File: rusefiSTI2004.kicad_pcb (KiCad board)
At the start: 2 copper layers, 138.6 x 113.6 mm, 35 parts, among them J1 1-1376430-0, M1 Module-mega-mcu144-0.7, M13 Module-knock-0.2, M14 Module-power_12and5V-0.3, M2 Module-motor-driver-0.1, M3 Module-wbo-0.5, M4 Module-can-0.1, M5 Module-vr-discrete-0.5, M6 Module-vr-discrete-0.5, M7 Module-knock-0.2, M8 Module-power_12and5V-0.3, M9 Module-motor-driver-0.1, Q1 VND14NV04-E, Q2 VND14NV04-E, Q3 VND14NV04-E, Q4 VND14NV04-E, Q5 VND14NV04-E, Q6 VND14NV04-E, Q7 VND14NV04-E, Q8 VND14NV04-E

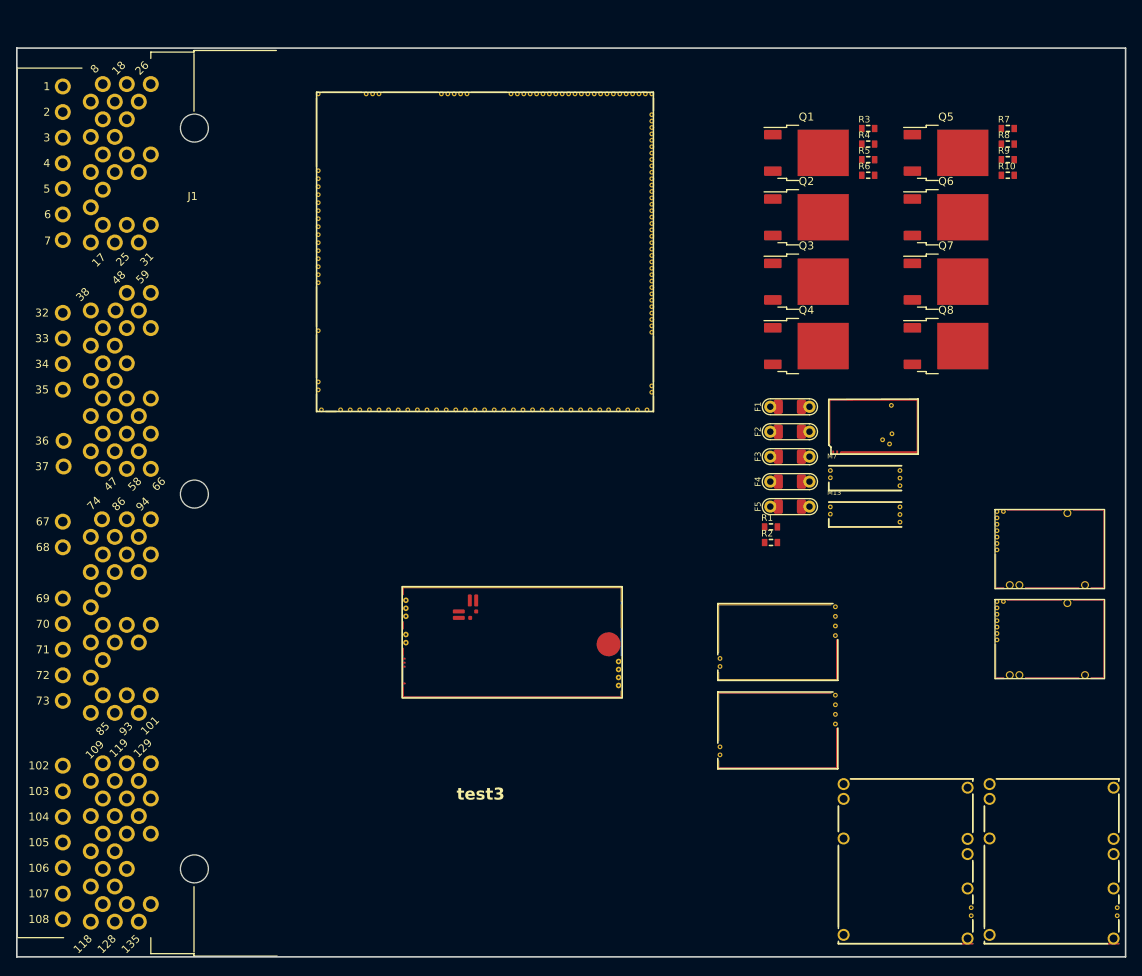
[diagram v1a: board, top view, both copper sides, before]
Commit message: PCB: update from schematic and first placement; H1-H4 M3 mounting holes; drop STI.pretty
- kicad-pcb-from-netlist (EmbeddedEra/KiCad scripting/pcb) rebuilt the rev-a board: 137 footprints,
  linked to their symbols (DRC schematic parity 0), nets on every pad, floorplan in pcb_place.json.
- H1-H4 added to the schematic (Aux sheet) first, then placed.
- STI.pretty removed: the board now uses EmbeddedEra_Library:TE_1-1376430-0.
- hellen-create-board builds the full package again (the F5 mismatch is gone).

Co-Authored-By: Claude Opus 5.5 <noreply@anthropic.com>
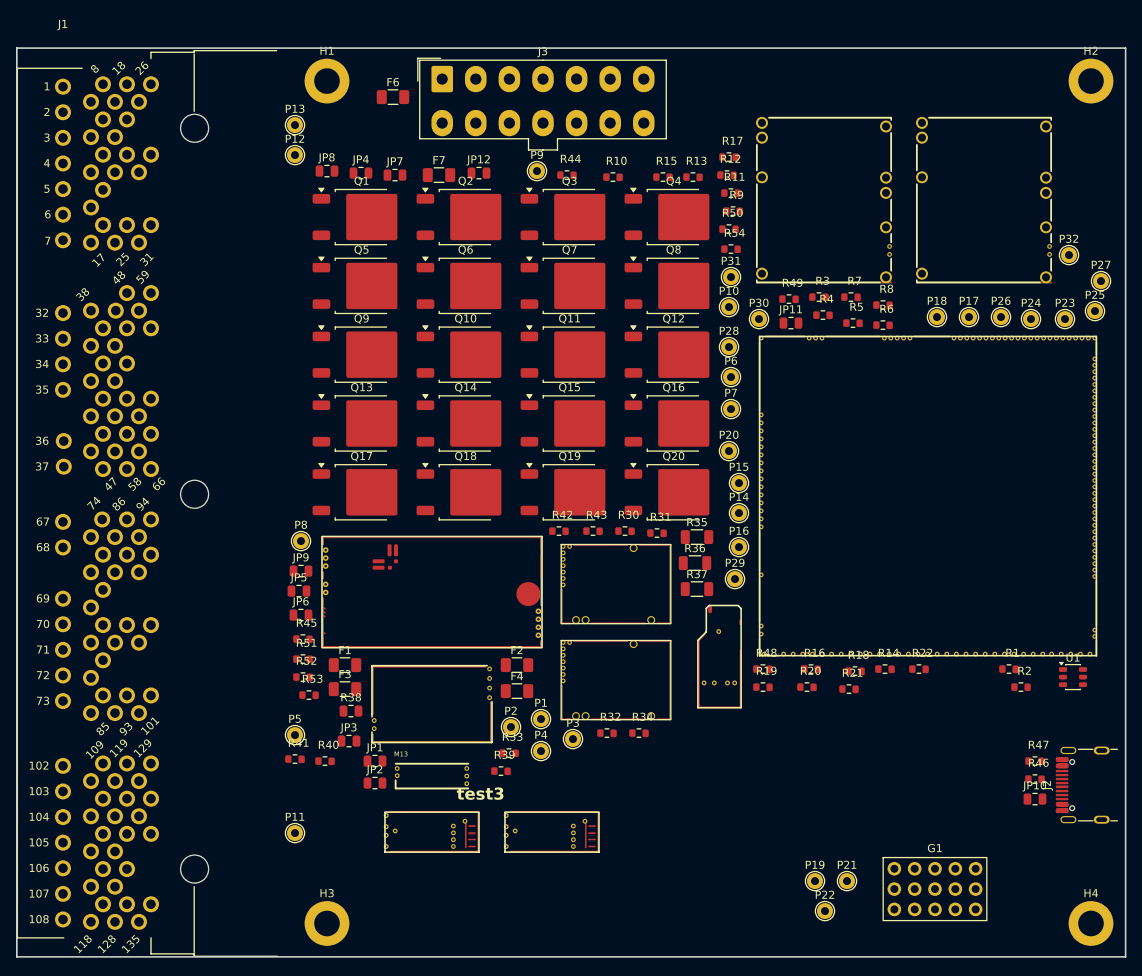
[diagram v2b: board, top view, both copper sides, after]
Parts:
- removed F5: nSMD005, hellen-one-common:PAD-1206-PAD
- removed M4: Module-can-0.1, hellen-one-can-0.1:can
- removed M6: Module-vr-discrete-0.5, hellen-one-vr-discrete-0.5:vr-discrete
- removed M7: Module-knock-0.2, hellen-one-knock-0.2:knock
- added F6: nSMD050-24V, EmbeddedEra_Library:Fuse_1206_3216Metric, F.Cu at (132.2, 42.0)
- added F7: JK-nSMD005, EmbeddedEra_Library:Fuse_1206_3216Metric, F.Cu at (138.0, 51.8)
- added G1: PROTO_AREA, EmbeddedEra_Library:PROTO_AREA_3x5_P2.54mm, F.Cu at (194.9, 138.5)
- added H1: MountingHole_3.2mm, EmbeddedEra_Library:MountingHole_3.2mm_M3_DIN965_Pad, F.Cu at (124.0, 40.0)
- added H2: MountingHole_3.2mm, EmbeddedEra_Library:MountingHole_3.2mm_M3_DIN965_Pad, F.Cu at (219.5, 40.0)
- added H3: MountingHole_3.2mm, EmbeddedEra_Library:MountingHole_3.2mm_M3_DIN965_Pad, F.Cu at (124.0, 145.3)
- added H4: MountingHole_3.2mm, EmbeddedEra_Library:MountingHole_3.2mm_M3_DIN965_Pad, F.Cu at (219.5, 145.3)
- added J2: USB C 2.0 16P, EmbeddedEra_Library:USB_C_Receptacle_HRO _TYPE-C-31-M-12, F.Cu at (218.6, 128.0)
- added J3: Molex_39281143, EmbeddedEra_Library:Molex_Mini-Fit_Jr_5566-14A_2x07_P4.20mm_Vertical, F.Cu at (138.4, 39.8)
- added JP1: 0, EmbeddedEra_Library:R_0805_2012Metric, F.Cu at (130.0, 125.0)
- added JP10: 0, EmbeddedEra_Library:R_0805_2012Metric, F.Cu at (212.5, 129.8)
- added JP11: 0, EmbeddedEra_Library:R_0805_2012Metric, F.Cu at (182.0, 70.2)
- added JP12: 0, EmbeddedEra_Library:R_0805_2012Metric, F.Cu at (143.0, 51.5)
- added JP2: 0, EmbeddedEra_Library:R_0805_2012Metric, F.Cu at (130.0, 127.8)
- added JP3: 0, EmbeddedEra_Library:R_0805_2012Metric, F.Cu at (126.8, 122.5)
- added JP4: 0, EmbeddedEra_Library:R_0805_2012Metric, F.Cu at (128.2, 51.5)
- added JP5: 0, EmbeddedEra_Library:R_0805_2012Metric, F.Cu at (120.5, 103.8)
- added JP6: 0, EmbeddedEra_Library:R_0805_2012Metric, F.Cu at (120.8, 106.8)
- added JP7: 0, EmbeddedEra_Library:R_0805_2012Metric, F.Cu at (132.5, 51.8)
- added JP8: 0, EmbeddedEra_Library:R_0805_2012Metric, F.Cu at (124.0, 51.2)
- added JP9: 0, EmbeddedEra_Library:R_0805_2012Metric, F.Cu at (120.8, 101.2)
- added M10: Module-lin-0.1, hellen-one-lin-0.1:lin, F.Cu at (170.3, 118.4)
- added M11: Module-dinput4-0.1, hellen-one-dinput4-0.1:dinput4, F.Cu at (131.2, 136.5)
- added M12: Module-dinput4-0.1, hellen-one-dinput4-0.1:dinput4, F.Cu at (146.2, 136.5)
- added P1: WBO_UN, EmbeddedEra_Library:TestPoint_THTPad_D2.0mm_Drill1.0mm, F.Cu at (150.8, 119.8)
- added P10: OUT_SPARE_LS2, EmbeddedEra_Library:TestPoint_THTPad_D2.0mm_Drill1.0mm, F.Cu at (174.2, 68.2)
- added P11: CHARGE_A22, EmbeddedEra_Library:TestPoint_THTPad_D2.0mm_Drill1.0mm, F.Cu at (120.0, 134.0)
- added P12: FP_STATUS, EmbeddedEra_Library:TestPoint_THTPad_D2.0mm_Drill1.0mm, F.Cu at (120.0, 49.2)
- added P13: DLC6_D29, EmbeddedEra_Library:TestPoint_THTPad_D2.0mm_Drill1.0mm, F.Cu at (120.0, 45.5)
- added P14: SPARE_IGN6, EmbeddedEra_Library:TestPoint_THTPad_D2.0mm_Drill1.0mm, F.Cu at (175.5, 94.0)
- added P15: SPARE_IGN7, EmbeddedEra_Library:TestPoint_THTPad_D2.0mm_Drill1.0mm, F.Cu at (175.5, 90.2)
- added P16: SPARE_IGN8, EmbeddedEra_Library:TestPoint_THTPad_D2.0mm_Drill1.0mm, F.Cu at (175.5, 98.2)
- added P17: I2C_1_SCL, EmbeddedEra_Library:TestPoint_THTPad_D2.0mm_Drill1.0mm, F.Cu at (204.2, 69.5)
- added P18: I2C_1_SDA, EmbeddedEra_Library:TestPoint_THTPad_D2.0mm_Drill1.0mm, F.Cu at (200.2, 69.5)
- added P19: +5VA, EmbeddedEra_Library:TestPoint_THTPad_D2.0mm_Drill1.0mm, F.Cu at (185.0, 140.0)
- added P2: WBO_VM, EmbeddedEra_Library:TestPoint_THTPad_D2.0mm_Drill1.0mm, F.Cu at (147.0, 120.8)
- added P20: +3.3V, EmbeddedEra_Library:TestPoint_THTPad_D2.0mm_Drill1.0mm, F.Cu at (174.2, 86.2)
- added P21: +12V_RAW, EmbeddedEra_Library:TestPoint_THTPad_D2.0mm_Drill1.0mm, F.Cu at (189.0, 140.0)
- added P22: GND, EmbeddedEra_Library:TestPoint_THTPad_D2.0mm_Drill1.0mm, F.Cu at (186.2, 143.8)
- added P23: BOOT0, EmbeddedEra_Library:TestPoint_THTPad_D2.0mm_Drill1.0mm, F.Cu at (216.2, 69.8)
- added P24: SWDIO, EmbeddedEra_Library:TestPoint_THTPad_D2.0mm_Drill1.0mm, F.Cu at (212.0, 69.8)
- added P25: SWCLK, EmbeddedEra_Library:TestPoint_THTPad_D2.0mm_Drill1.0mm, F.Cu at (220.0, 68.8)
- added P26: NRST, EmbeddedEra_Library:TestPoint_THTPad_D2.0mm_Drill1.0mm, F.Cu at (208.2, 69.5)
- added P27: SPARE_PWM3, EmbeddedEra_Library:TestPoint_THTPad_D2.0mm_Drill1.0mm, F.Cu at (220.8, 65.0)
- added P28: SPARE_RES2, EmbeddedEra_Library:TestPoint_THTPad_D2.0mm_Drill1.0mm, F.Cu at (174.2, 73.2)
- added P29: AUX_IN1, EmbeddedEra_Library:TestPoint_THTPad_D2.0mm_Drill1.0mm, F.Cu at (175.0, 102.2)
- added P3: WBO_IP, EmbeddedEra_Library:TestPoint_THTPad_D2.0mm_Drill1.0mm, F.Cu at (154.8, 122.2)
- added P30: AUX_IN2, EmbeddedEra_Library:TestPoint_THTPad_D2.0mm_Drill1.0mm, F.Cu at (178.0, 69.8)
- added P31: AUX_IN3, EmbeddedEra_Library:TestPoint_THTPad_D2.0mm_Drill1.0mm, F.Cu at (174.5, 64.5)
- added P32: PG_5VP_APS, EmbeddedEra_Library:TestPoint_THTPad_D2.0mm_Drill1.0mm, F.Cu at (216.8, 61.8)
- added P4: WBO_RTRIM, EmbeddedEra_Library:TestPoint_THTPad_D2.0mm_Drill1.0mm, F.Cu at (150.8, 123.8)
- added P5: WBO_HEATER, EmbeddedEra_Library:TestPoint_THTPad_D2.0mm_Drill1.0mm, F.Cu at (120.0, 121.8)
- added P6: CAN_H, EmbeddedEra_Library:TestPoint_THTPad_D2.0mm_Drill1.0mm, F.Cu at (174.5, 77.0)
- added P7: CAN_L, EmbeddedEra_Library:TestPoint_THTPad_D2.0mm_Drill1.0mm, F.Cu at (174.5, 81.0)
- added P8: K_LINE, EmbeddedEra_Library:TestPoint_THTPad_D2.0mm_Drill1.0mm, F.Cu at (120.8, 97.5)
- added P9: OUT_SPARE_LS1, EmbeddedEra_Library:TestPoint_THTPad_D2.0mm_Drill1.0mm, F.Cu at (150.2, 51.2)
- added Q10: NCV8401BDTRKG, EmbeddedEra_Library:TO-252-2, F.Cu at (141.3, 74.2)
- added Q11: NCV8401BDTRKG, EmbeddedEra_Library:TO-252-2, F.Cu at (154.3, 74.2)
- added Q12: NCV8401BDTRKG, EmbeddedEra_Library:TO-252-2, F.Cu at (167.3, 74.2)
- added Q13: NCV8401BDTRKG, EmbeddedEra_Library:TO-252-2, F.Cu at (128.3, 82.8)
- added Q14: NCV8401BDTRKG, EmbeddedEra_Library:TO-252-2, F.Cu at (141.3, 82.8)
- added Q15: NCV8401BDTRKG, EmbeddedEra_Library:TO-252-2, F.Cu at (154.3, 82.8)
- added Q16: NCV8401BDTRKG, EmbeddedEra_Library:TO-252-2, F.Cu at (167.3, 82.8)
- added Q17: NCV8401BDTRKG, EmbeddedEra_Library:TO-252-2, F.Cu at (128.3, 91.4)
- added Q18: NCV8401BDTRKG, EmbeddedEra_Library:TO-252-2, F.Cu at (141.3, 91.4)
- added Q19: NCV8401BDTRKG, EmbeddedEra_Library:TO-252-2, F.Cu at (154.3, 91.4)
- added Q20: NCV8401BDTRKG, EmbeddedEra_Library:TO-252-2, F.Cu at (167.3, 91.4)
- added Q9: NCV8401BDTRKG, EmbeddedEra_Library:TO-252-2, F.Cu at (128.3, 74.2)
- added R11: 4.7K, EmbeddedEra_Library:R_0603_1608Metric, F.Cu at (174.5, 54.0)
- added R12: 4.7K, EmbeddedEra_Library:R_0603_1608Metric, F.Cu at (174.0, 51.8)
- added R13: 4.7K, EmbeddedEra_Library:R_0603_1608Metric, F.Cu at (169.8, 52.0)
- added R14: 4.7K, EmbeddedEra_Library:R_0603_1608Metric, F.Cu at (193.8, 113.5)
- added R15: 4.7K, EmbeddedEra_Library:R_0603_1608Metric, F.Cu at (166.0, 52.0)
- added R16: 4.7K, EmbeddedEra_Library:R_0603_1608Metric, F.Cu at (184.5, 113.5)
- added R17: 4.7K, EmbeddedEra_Library:R_0603_1608Metric, F.Cu at (174.2, 49.5)
- added R18: 4.7K, EmbeddedEra_Library:R_0603_1608Metric, F.Cu at (190.0, 113.8)
- added R19: 4.7K, EmbeddedEra_Library:R_0603_1608Metric, F.Cu at (178.5, 115.8)
- added R20: 4.7K, EmbeddedEra_Library:R_0603_1608Metric, F.Cu at (184.0, 115.8)
- added R21: 4.7K, EmbeddedEra_Library:R_0603_1608Metric, F.Cu at (189.2, 116.0)
- added R22: 4.7K, EmbeddedEra_Library:R_0603_1608Metric, F.Cu at (198.0, 113.5)
- added R30: 4.7K, EmbeddedEra_Library:R_0603_1608Metric, F.Cu at (161.2, 96.2)
- added R31: 4.7K, EmbeddedEra_Library:R_0603_1608Metric, F.Cu at (165.2, 96.5)
- added R32: 4.7K, EmbeddedEra_Library:R_0603_1608Metric, F.Cu at (159.0, 121.5)
- added R33: 4.7K, EmbeddedEra_Library:R_0603_1608Metric, F.Cu at (146.8, 124.0)
- added R34: 4.7K, EmbeddedEra_Library:R_0603_1608Metric, F.Cu at (163.0, 121.5)
- added R35: 1K, EmbeddedEra_Library:R_1206_3216Metric, F.Cu at (170.2, 97.0)
- added R36: 1K, EmbeddedEra_Library:R_1206_3216Metric, F.Cu at (170.0, 100.2)
- added R37: 1K, EmbeddedEra_Library:R_1206_3216Metric, F.Cu at (170.2, 103.5)
- added R38: 2.2k, EmbeddedEra_Library:R_0805_2012Metric, F.Cu at (127.0, 118.8)
- added R39: 100, EmbeddedEra_Library:R_0603_1608Metric, F.Cu at (145.8, 126.2)
- added R40: 1K, EmbeddedEra_Library:R_0603_1608Metric, F.Cu at (123.8, 125.0)
- added R41: 10K, EmbeddedEra_Library:R_0603_1608Metric, F.Cu at (120.0, 124.8)
- added R42: 1K, EmbeddedEra_Library:R_0603_1608Metric, F.Cu at (153.0, 96.2)
- added R43: 1K, EmbeddedEra_Library:R_0603_1608Metric, F.Cu at (157.2, 96.2)
- added R44: 4.7K, EmbeddedEra_Library:R_0603_1608Metric, F.Cu at (154.0, 51.8)
- added R45: 1K, EmbeddedEra_Library:R_0603_1608Metric, F.Cu at (121.0, 109.8)
- added R46: 5.1K, EmbeddedEra_Library:R_0603_1608Metric, F.Cu at (212.5, 127.2)
- added R47: 5.1K, EmbeddedEra_Library:R_0603_1608Metric, F.Cu at (212.5, 125.0)
- added R48: 4.7K, EmbeddedEra_Library:R_0603_1608Metric, F.Cu at (178.5, 113.5)
- added R49: 4.7K, EmbeddedEra_Library:R_0603_1608Metric, F.Cu at (181.8, 67.2)
- added R50: 4.7K, EmbeddedEra_Library:R_0603_1608Metric, F.Cu at (174.2, 58.5)
- added R51: 10K, EmbeddedEra_Library:R_0603_1608Metric, F.Cu at (121.0, 112.2)
- added R52: 10K, EmbeddedEra_Library:R_0603_1608Metric, F.Cu at (121.0, 114.5)
- added R53: 10K, EmbeddedEra_Library:R_0603_1608Metric, F.Cu at (121.8, 116.8)
- added R54: 120, EmbeddedEra_Library:R_0603_1608Metric, F.Cu at (174.5, 61.0)
- added U1: USBLC6-2SC6, EmbeddedEra_Library:SOT-23-6, F.Cu at (217.2, 114.5)
- F1, F2, F3, F4: value nSMD005 -> JK-nSMD005; footprint hellen-one-common:PAD-1206-PAD -> EmbeddedEra_Library:Fuse_1206_3216Metric
- J1: value 1-1376430-0 -> TE_1-1376430-0; footprint STI:1-1376430-0 -> EmbeddedEra_Library:TE_1-1376430-0
- Q1, Q2, Q3, Q4, Q5, Q6, Q7, Q8: value VND14NV04-E -> NCV8401BDTRKG; footprint hellen-one-common:DPAK -> EmbeddedEra_Library:TO-252-2
- R1: value 33k -> 33K; footprint hellen-one-common:R0603 -> EmbeddedEra_Library:R_0603_1608Metric
- R10, R3, R4, R5, R6, R7, R8, R9: value 4.7k -> 4.7K; footprint hellen-one-common:R0603 -> EmbeddedEra_Library:R_0603_1608Metric
- R2: value 6.8k -> 6.8K; footprint hellen-one-common:R0603 -> EmbeddedEra_Library:R_0603_1608Metric
- moved M14 87.4 mm to (177.6, 65.3)
- moved M8 83.2 mm to (197.6, 65.3)
- moved Q5 73.8 mm to (128.3, 65.6)
- moved F1 64.3 mm to (126.2, 113.0)
- moved M13 63.3 mm to (132.5, 128.5)
- moved M1 63.2 mm to (178.0, 111.9)
- moved F3 62.7 mm to (126.2, 116.0)
- moved Q6 59.6 mm to (141.3, 65.6)
- moved Q1 55.1 mm to (128.3, 57.0)
- moved M9 54.5 mm to (153.2, 119.9)
- moved M2 54.4 mm to (153.2, 107.9)
- moved R10 49.4 mm to (159.8, 52.0)
- moved Q7 45.9 mm to (154.3, 65.6)
- moved F2 44.9 mm to (147.8, 113.0)
- moved M5 43.9 mm to (129.5, 122.8)
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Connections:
- net /ELECTRONIC_THROTTE_RELAY renamed ELECTRONIC_THROTTE_RELAY
- net /FAN_RELAY_1 renamed FAN_RELAY_1
- net /IGN renamed IGN
- net /INJ1 renamed INJ1
- net /INJ2 renamed INJ2
- net /INJ3 renamed INJ3
- net /INJ4 renamed INJ4
- net /IN_CRANK renamed IN_CRANK
- net /IN_CRANK+ renamed IN_CRANK+
- net /IN_ECT renamed IN_ECT
- net /IN_IAT renamed IN_IAT
- net /IN_KNOCK renamed IN_KNOCK
- net /IN_KNOCK_RAW renamed IN_KNOCK_RAW
- net /IN_PPS_MAIN renamed IN_PPS_MAIN
- net /IN_PPS_SUB renamed IN_PPS_SUB
- net /IN_TPS_MAIN renamed IN_TPS_MAIN
- net /IN_TPS_SUB renamed IN_TPS_SUB
- net /IN_VMAIN renamed IN_VMAIN
- net /MAIN_RELAY renamed MAIN_RELAY
- net /OUT_ELECTRONIC_THROTTE_RELAY renamed OUT_ELECTRONIC_THROTTE_RELAY
- net /OUT_ETB+ renamed OUT_ETB+
- net /OUT_ETB- renamed OUT_ETB-
- net /OUT_FAN_RELAY_1 renamed OUT_FAN_RELAY_1
- net /OUT_FAN_RELAY_2 renamed OUT_FAN_RELAY_2
- net /OUT_IGN2 renamed OUT_IGN2
- net /OUT_INJ1 renamed OUT_INJ1
- net /OUT_INJ2 renamed OUT_INJ2
- net /OUT_INJ3 renamed OUT_INJ3
- net /OUT_INJ4 renamed OUT_INJ4
- net /OUT_MAIN_RELAY renamed OUT_MAIN_RELAY
- net /PG_5VP renamed PG_5VP
- net /THRESHOLD_VR_CR renamed THRESHOLD_VR_CR
- net /VBAT renamed VBAT
- net /VREF renamed VREF
- net /VR_ANALOG_CR renamed VR_ANALOG_CR
- net Net-(F1-Pad1) renamed /Vehicle connector/IGN4_COIL
- net Net-(F2-Pad1) renamed /Vehicle connector/IGN3_COIL
- net Net-(F3-Pad1) renamed /Vehicle connector/IGN2_COIL
- net Net-(F4-Pad1) renamed /Vehicle connector/IGN1_COIL
- F1 pad 2: /OUT_IGN4 -> OUT_IGN4
- F2 pad 2: /OUT_IGN3 -> OUT_IGN3
- F4 pad 2: /OUT_IGN1 -> OUT_IGN1
- J1 pad 10: /IN_PS_PRESSURE_SWIITCH -> IN_PS_PRESSURE_SWITCH
- J1 pad 102: /IN_CLT -> IN_CLUTCH
- J1 pad 103: unconnected-(J1-Pad103) -> WBO_HEATER
- J1 pad 104: unconnected-(J1-Pad104) -> WBO_HEATER
- J1 pad 109: unconnected-(J1-Pad109) -> OUT_TGV_CLOSE
- J1 pad 11: unconnected-(J1-Pad11) -> IN_DEFOG
- J1 pad 110: unconnected-(J1-Pad110) -> OUT_TGV_OPEN
- J1 pad 111: unconnected-(J1-Pad111) -> OUT_TGV_CLOSE
- J1 pad 112: unconnected-(J1-Pad112) -> OUT_TGV_OPEN
- J1 pad 113: unconnected-(J1-Pad113) -> EVAP_A12
- J1 pad 114: unconnected-(J1-Pad114) -> EVAP_A13
- J1 pad 115: /OUT_PURGE_CONTROL -> OUT_PURGE_CONTROL
- J1 pad 116: unconnected-(J1-Pad116) -> OUT_CRUISE_MAIN_LIGHT
- J1 pad 117: unconnected-(J1-Pad117) -> OUT_CRUISE_SET_LIGHT
- J1 pad 118: unconnected-(J1-Pad118) -> OUT_MIL
- J1 pad 119: /OUT_VVT_RH+ -> +12V_RAW
- J1 pad 12: unconnected-(J1-Pad12) -> IN_SMALL_LIGHT
- J1 pad 120: /OUT_VVT_LH+ -> +12V_RAW
- J1 pad 123: unconnected-(J1-Pad123) -> CHARGE_A22
- J1 pad 124: /OUT_TACH -> OUT_TACH
- J1 pad 126: unconnected-(J1-Pad126) -> WBO_IP_J1
- J1 pad 127: unconnected-(J1-Pad127) -> WBO_VM_J1
- J1 pad 129: /OUT_VVT_RH- -> OUT_VVT_RH-
- J1 pad 13: unconnected-(J1-Pad13) -> IN_BLOWER
- J1 pad 130: /OUT_VVT_LH- -> OUT_VVT_LH-
- J1 pad 133: /OUT_WG -> OUT_WG
- J1 pad 134: unconnected-(J1-Pad134) -> WBO_UN_J1
- J1 pad 135: unconnected-(J1-Pad135) -> GND
- J1 pad 14: unconnected-(J1-Pad14) -> IN_TEST_MODE
- J1 pad 16: unconnected-(J1-Pad16) -> IN_AC_REQUEST
- J1 pad 20: unconnected-(J1-Pad20) -> K_LINE
- J1 pad 22: /IN_CRANK- -> unconnected-(J1-Pad22)
- J1 pad 24: unconnected-(J1-Pad24) -> IN_BLOWBY
- J1 pad 25: unconnected-(J1-Pad25) -> IN_O2S
- J1 pad 28: /FUEL_PUMP_SIGNAL2 -> FP_STATUS
- J1 pad 29: unconnected-(J1-Pad29) -> DLC6_D29
- J1 pad 38: unconnected-(J1-Pad38) -> IN_CRUISE_MAIN
- J1 pad 39: unconnected-(J1-Pad39) -> IN_BRAKE_SW2
- J1 pad 40: unconnected-(J1-Pad40) -> IN_BRAKE_SW1
- J1 pad 41: unconnected-(J1-Pad41) -> IN_CRUISE_RESUME
- J1 pad 42: unconnected-(J1-Pad42) -> IN_CRUISE_SET
- J1 pad 46: /APS_PS_5V -> APS_PS_5V
- J1 pad 47: /SENSOR_PS_5V -> +5VAS
- J1 pad 51: /IN_FUEL_LEVEL -> IN_FUEL_LEVEL
- J1 pad 53: unconnected-(J1-Pad53) -> IN_MAP
- J1 pad 54: /IN_MAP -> IN_MAF
- J1 pad 57: /IN_TUMBLE_SENSOR_LH -> IN_TUMBLE_SENSOR_LH
- J1 pad 58: /IN_TUMBLE_SENSOR_RH -> IN_TUMBLE_SENSOR_RH
- J1 pad 6: Net-(F5-Pad1) -> +12V_ETB
- J1 pad 62: GND -> GND_SENSOR
- J1 pad 65: GND -> GND_SENSOR
- J1 pad 66: GND -> GND_SENSOR
- J1 pad 68: unconnected-(J1-Pad68) -> OUT_O2_HEATER_REAR
- J1 pad 7: /GND_INJECTORS -> GND
- J1 pad 74: /IN_CAM_HALL_CAM_LH -> IN_CAM
- J1 pad 75: /IN_CAM_HALL_CAM_RH -> IN_CAM_RH
- J1 pad 8: /IN_STARTER_SWITCH -> IN_STARTER_SWITCH
- J1 pad 88: /IN_CRANK- -> IN_CRANK-
- J1 pad 9: /IN_NEUTRAL_SWITCH -> IN_NEUTRAL_SWITCH
- J1 pad 92: /FUEL_PUMP_SIGNAL1 -> FUEL_PUMP_SIGNAL1
- J1 pad 93: /IN_VSS -> IN_VSS
- J1 pad 99: unconnected-(J1-Pad99) -> OUT_AC_RELAY
- M1 pad E10: unconnected-(M1-OUT_IO10-PadE10) -> DIN_AUX2
- M1 pad E11: unconnected-(M1-OUT_IO9-PadE11) -> DIN_AUX1
- M1 pad E12: unconnected-(M1-OUT_IO2-PadE12) -> O2_HEATER_REAR
- M1 pad E13: unconnected-(M1-OUT_IO12-PadE13) -> TGV_PWM
- M1 pad E14: unconnected-(M1-OUT_PWM5-PadE14) -> VVT_LH
- M1 pad E15: unconnected-(M1-OUT_PWM4-PadE15) -> VVT_RH
- M1 pad E16: unconnected-(M1-OUT_PWM3-PadE16) -> SPARE_PWM3
- M1 pad E17: /ETB_PWM -> ETB_PWM
- M1 pad E20: unconnected-(M1-OUT_IO13-PadE20) -> DIN_TEST_MODE
- M1 pad E21: unconnected-(M1-OUT_IO4-PadE21) -> TACH
- M1 pad E22: unconnected-(M1-OUT_IO8-PadE22) -> SPARE_LS2
- M1 pad E23: unconnected-(M1-OUT_IO7-PadE23) -> SPARE_LS1
- M1 pad E24: unconnected-(M1-OUT_IO11-PadE24) -> DIN_AUX3
- M1 pad E25: unconnected-(M1-OUT_PWM7-PadE25) -> PURGE
- M1 pad E27: unconnected-(M1-OUT_PWM1-PadE27) -> WG
- M1 pad E33: /FAN_RELAY_2 -> FAN_RELAY_2
- M1 pad E34: /FAN_RELAY_2 -> DIN_BLOWBY
- M1 pad E35: unconnected-(M1-IO6-PadE35) -> DIN_SMALL_LIGHT
- M1 pad E36: unconnected-(M1-IO7-PadE36) -> DIN_BLOWER
- M1 pad E6: unconnected-(M1-OUT_IO3-PadE6) -> AC_RELAY
- M1 pad E7: unconnected-(M1-OUT_IO5-PadE7) -> CRUISE_MAIN_LIGHT
- M1 pad E8: unconnected-(M1-OUT_IO1-PadE8) -> MIL
- M1 pad E9: unconnected-(M1-OUT_IO6-PadE9) -> CRUISE_SET_LIGHT
- M1 pad G: unconnected-(M1-GND-PadG) -> GND
- M1 pad N14: unconnected-(M1-I2C_SCL-PadN14) -> I2C_1_SCL
- M1 pad N15: unconnected-(M1-I2C_SDA-PadN15) -> I2C_1_SDA
- M1 pad N16: /ETB_DIR -> ETB_DIR
- M1 pad N19: /ETB_DIS -> ETB_DIS
- M1 pad N2: unconnected-(M1-USBM-PadN2) -> USB_D-
- M1 pad N20: unconnected-(M1-IO4-PadN20) -> TGV_DIS
- M1 pad N21: unconnected-(M1-IO3-PadN21) -> TGV_DIR
- M1 pad N23: unconnected-(M1-IO5-PadN23) -> DIN_DEFOG
- M1 pad N24: unconnected-(M1-UART8_RX-PadN24) -> UART_8_RX
- M1 pad N25: unconnected-(M1-UART8_TX-PadN25) -> UART_8_TX
- M1 pad N29: /PWR_EN -> PWR_EN
- M1 pad N3: unconnected-(M1-USBP-PadN3) -> USB_D+
- M1 pad N4: unconnected-(M1-VBUS-PadN4) -> USB_VBUS
- M1 pad N5: unconnected-(M1-BOOT0-PadN5) -> BOOT0
- M1 pad N7: unconnected-(M1-SWDIO-PadN7) -> SWDIO
- M1 pad N8: unconnected-(M1-SWCLK-PadN8) -> SWCLK
- M1 pad N9: unconnected-(M1-nReset-PadN9) -> NRST
- M1 pad S1: unconnected-(M1-IN_D4-PadS1) -> IN_CRUISE_SET
- M1 pad S11: unconnected-(M1-IN_AUX3-PadS11) -> IN_PS_PRESSURE_SWITCH
- M1 pad S12: unconnected-(M1-IN_AUX2-PadS12) -> IN_NEUTRAL_SWITCH
- M1 pad S13: unconnected-(M1-IN_AUX1-PadS13) -> IN_CAM_RH
- M1 pad S14: unconnected-(M1-IN_RES2-PadS14) -> SPARE_RES2
- M1 pad S15: unconnected-(M1-IN_O2S2-PadS15) -> IN_BRAKE_SW1
- M1 pad S16: unconnected-(M1-IN_O2S-PadS16) -> IN_O2S
- M1 pad S17: unconnected-(M1-IN_RES1-PadS17) -> IN_CLUTCH
- M1 pad S19: unconnected-(M1-IN_MAP3-PadS19) -> IN_TUMBLE_SENSOR_RH
- M1 pad S2: unconnected-(M1-IN_D3-PadS2) -> IN_CRUISE_RESUME
- M1 pad S20: unconnected-(M1-IN_MAP2-PadS20) -> IN_TUMBLE_SENSOR_LH
- M1 pad S21: /IN_MAP -> IN_MAP
- M1 pad S24: unconnected-(M1-IN_CAM-PadS24) -> IN_CAM
- M1 pad S25: unconnected-(M1-IN_VSS-PadS25) -> IN_VSS
- M1 pad S27: unconnected-(M1-IN_AT1-PadS27) -> IN_FUEL_LEVEL
- M1 pad S29: unconnected-(M1-IN_AT2-PadS29) -> AUX_AN2
- M1 pad S4: unconnected-(M1-IN_D1-PadS4) -> IN_CRUISE_MAIN
- M1 pad S6: unconnected-(M1-IN_SENS4-PadS6) -> IN_BRAKE_SW2
- M1 pad S7: unconnected-(M1-IN_SENS3-PadS7) -> IN_AC_REQUEST
- M1 pad S8: unconnected-(M1-IN_SENS2-PadS8) -> IN_STARTER_SWITCH
- M1 pad S9: unconnected-(M1-IN_SENS1-PadS9) -> IN_MAF
- M1 pad W11: /OUT_IGN1 -> OUT_IGN1
- M1 pad W12: unconnected-(M1-CANH-PadW12) -> CAN_H
- M1 pad W13: unconnected-(M1-CANL-PadW13) -> CAN_L
- M1 pad W4: unconnected-(M1-IGN8-PadW4) -> SPARE_IGN8
- M1 pad W5: unconnected-(M1-IGN7-PadW5) -> SPARE_IGN7
- M1 pad W6: unconnected-(M1-IGN6-PadW6) -> SPARE_IGN6
- M1 pad W7: unconnected-(M1-IGN5-PadW7) -> FP_CMD
- M1 pad W8: /OUT_IGN1 -> OUT_IGN4
- M1 pad W9: /OUT_IGN1 -> OUT_IGN3
- M14 pad E5: /PWR_EN -> PWR_EN
- M2 pad W1: /ETB_PWM -> ETB_DIS
- M2 pad W2: /ETB_DIR -> ETB_PWM
- M2 pad W4: /ETB_DIS -> ETB_DIR
- M3 pad E1: unconnected-(M3-LSU_Un-PadE1) -> WBO_UN
- M3 pad E2: unconnected-(M3-LSU_Vm-PadE2) -> WBO_VM
- M3 pad E3: unconnected-(M3-LSU_Ip-PadE3) -> WBO_IP
- M3 pad E4: unconnected-(M3-LSU_Rtrim-PadE4) -> WBO_RTRIM
- M3 pad E5: unconnected-(M3-LSU_H+-PadE5) -> WBO_HEATER
- M3 pad E6: unconnected-(M3-LSU_H--PadE6) -> GND
- M3 pad G: unconnected-(M3-GND-PadG) -> GND
- M3 pad J1: unconnected-(M3-SEL1-PadJ1) -> WBO_SEL1
- M3 pad J_GND1: unconnected-(M3-PULL_DOWN1-PadJ_GND1) -> WBO_SEL1
- M3 pad W1: unconnected-(M3-V5_IN-PadW1) -> +5VA
- M3 pad W3: unconnected-(M3-CANL-PadW3) -> CAN_L
- M3 pad W4: unconnected-(M3-CANH-PadW4) -> CAN_H
- M5 pad W1: /IN_CRANK- -> IN_CRANK-
- M8 pad E5: unconnected-(M8-EN_5VP-PadE5) -> PWR_EN
- M8 pad E6: unconnected-(M8-PG_5VP-PadE6) -> PG_5VP_APS
- M8 pad S1: unconnected-(M8-GND-PadS1) -> GND
- M8 pad V1: unconnected-(M8-V12_PERM-PadV1) -> +12V_BACK_UP
- M8 pad V2: unconnected-(M8-IN_VIGN-PadV2) -> +12V_IGN
- M8 pad V3: unconnected-(M8-V12_RAW-PadV3) -> +12V_RAW
- M8 pad V4: unconnected-(M8-5VP-PadV4) -> APS_PS_5V
- M9 pad G: unconnected-(M9-GND-PadG) -> GND
- M9 pad N2: unconnected-(M9-12V_IN-PadN2) -> +12V_RAW
- M9 pad S1: unconnected-(M9-12V_IN-PadS1) -> +12V_RAW
- M9 pad S2: unconnected-(M9-OUT--PadS2) -> OUT_TGV_CLOSE
- M9 pad S3: unconnected-(M9-OUT+-PadS3) -> OUT_TGV_OPEN
- M9 pad W1: unconnected-(M9-DIS-PadW1) -> TGV_DIS
- M9 pad W2: unconnected-(M9-PWM-PadW2) -> TGV_PWM
- M9 pad W4: unconnected-(M9-DIR-PadW4) -> TGV_DIR
- M9 pad W5: unconnected-(M9-3V3_IN-PadW5) -> +3.3V
- Q7 pad 1: /FAN_RELAY_2 -> FAN_RELAY_2
- R9 pad 1: /FAN_RELAY_2 -> FAN_RELAY_2
